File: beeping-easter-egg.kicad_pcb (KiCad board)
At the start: 2 copper layers, 38 x 38 mm, 17 parts, among them Q1 AO3401A, Q2 AO3401A, SW1 YUEN FUNG ST-0-102-A01-T000-LF, U1 TLC555CDR

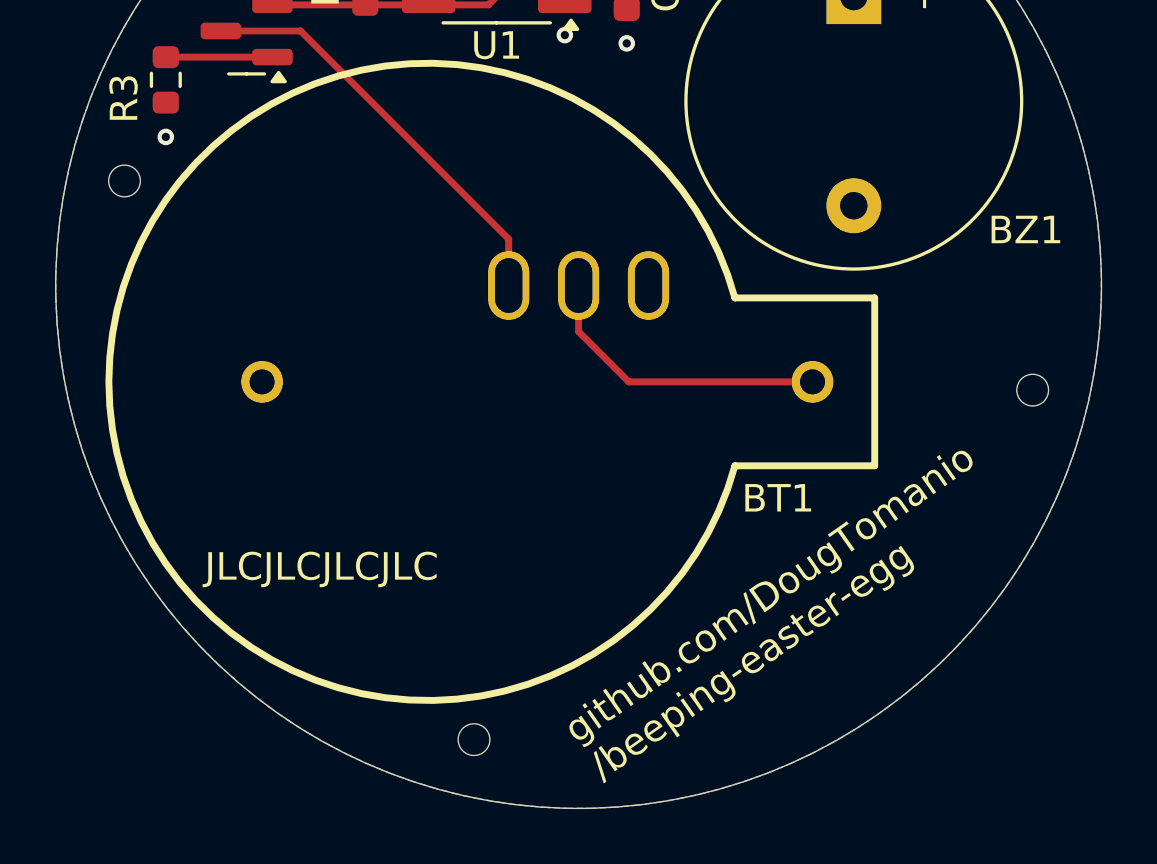
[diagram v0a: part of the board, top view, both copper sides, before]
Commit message: Remove tooling holes. They are added to the panelization frame instead.
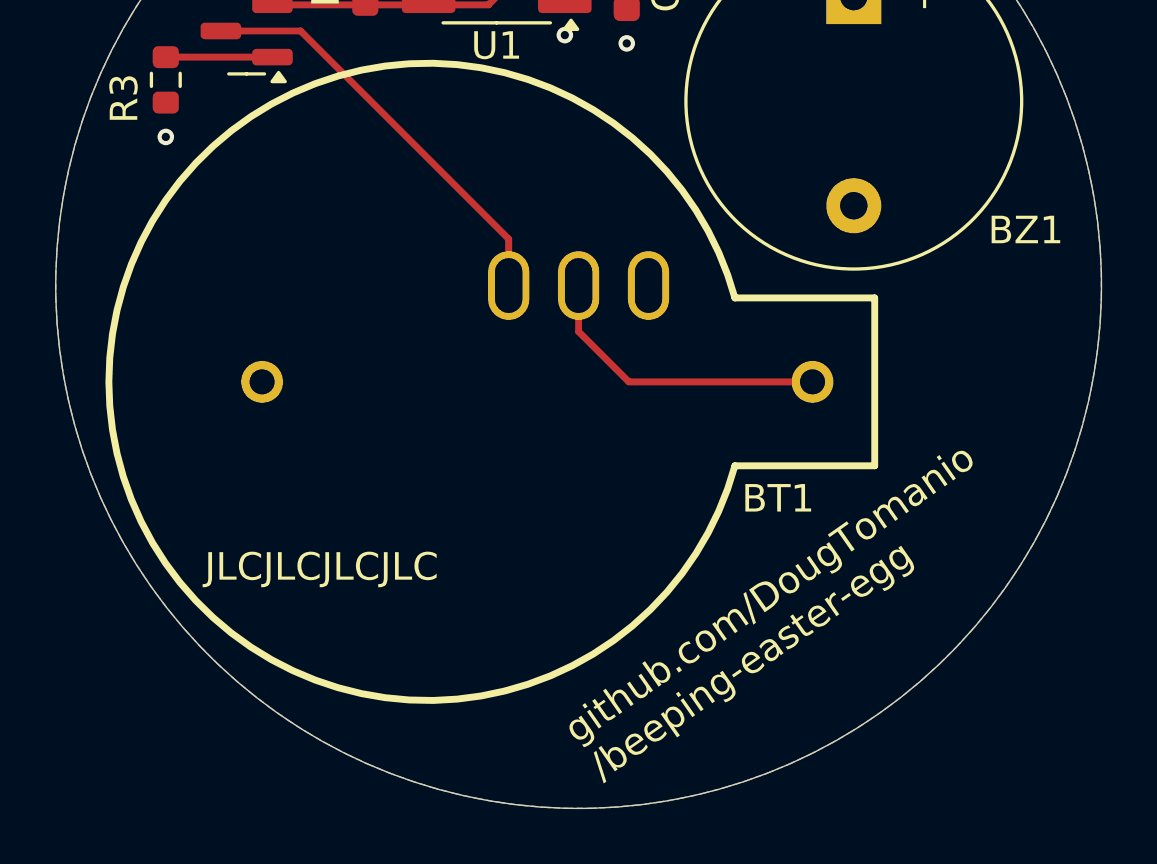
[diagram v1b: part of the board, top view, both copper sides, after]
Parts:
- removed H1, H2, H3: MountingHole, MountingHole:ToolingHole_1.152mm

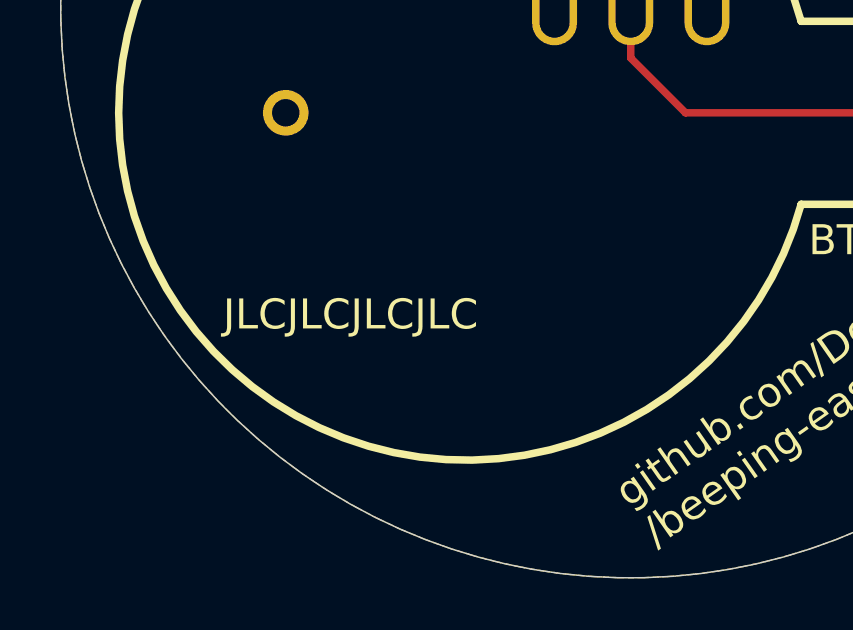
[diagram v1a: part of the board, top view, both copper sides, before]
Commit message: Remove jlc order number placeholder. It is added to the panelization frame instead.
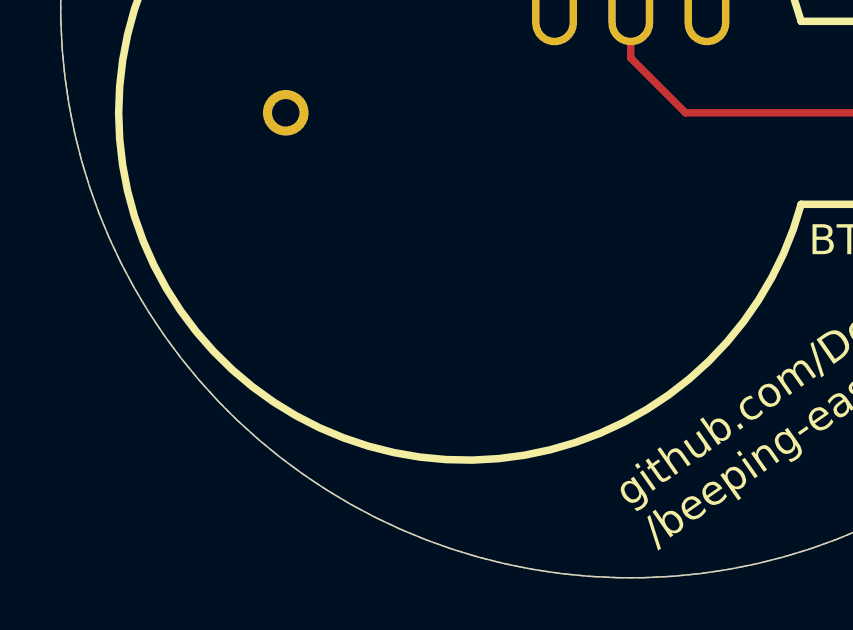
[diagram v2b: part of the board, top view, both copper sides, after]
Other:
- board text removed: "JLCJLCJLCJLC"
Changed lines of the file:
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@@
-		)
-	)
-	(gr_text "JLCJLCJLCJLC"
-		(at 136.41 110.81 0)
-		(layer "F.SilkS")
-		(effects
-			(font
-				(size 1 1)
-				(thickness 0.15)
-			)
-			(justify left bottom)
 		)
 	)

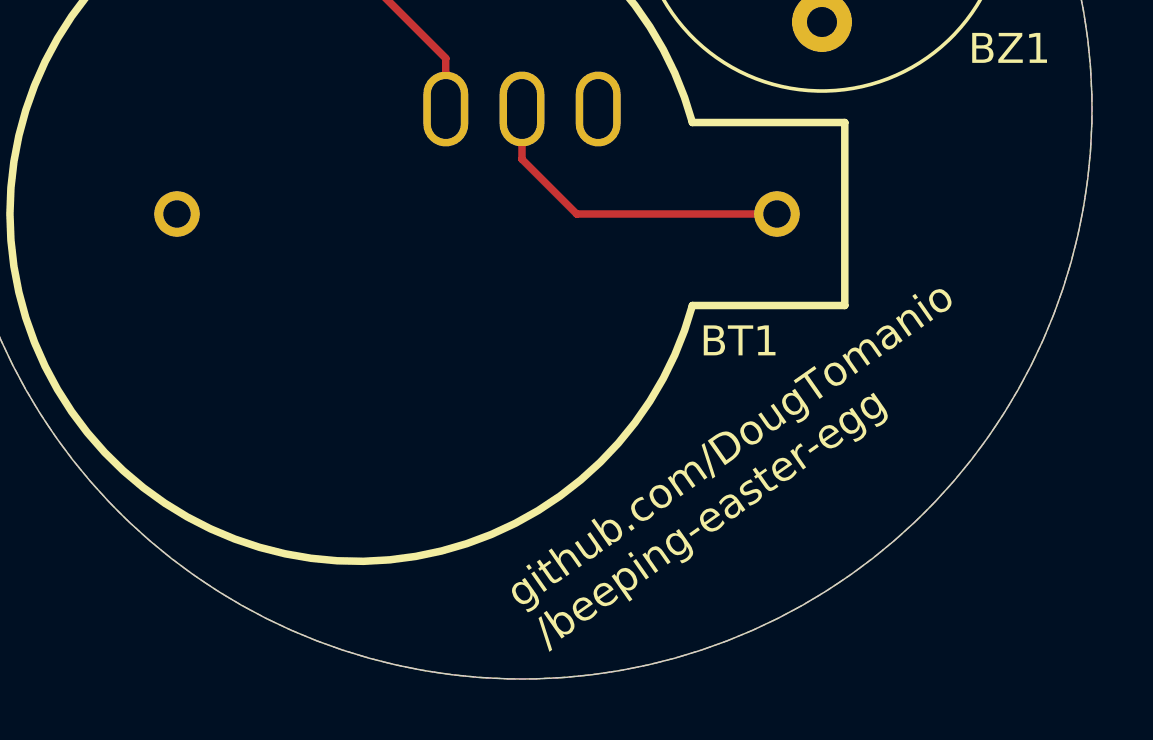
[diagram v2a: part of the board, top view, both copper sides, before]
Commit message: Move label to back copper. Add Rev number.
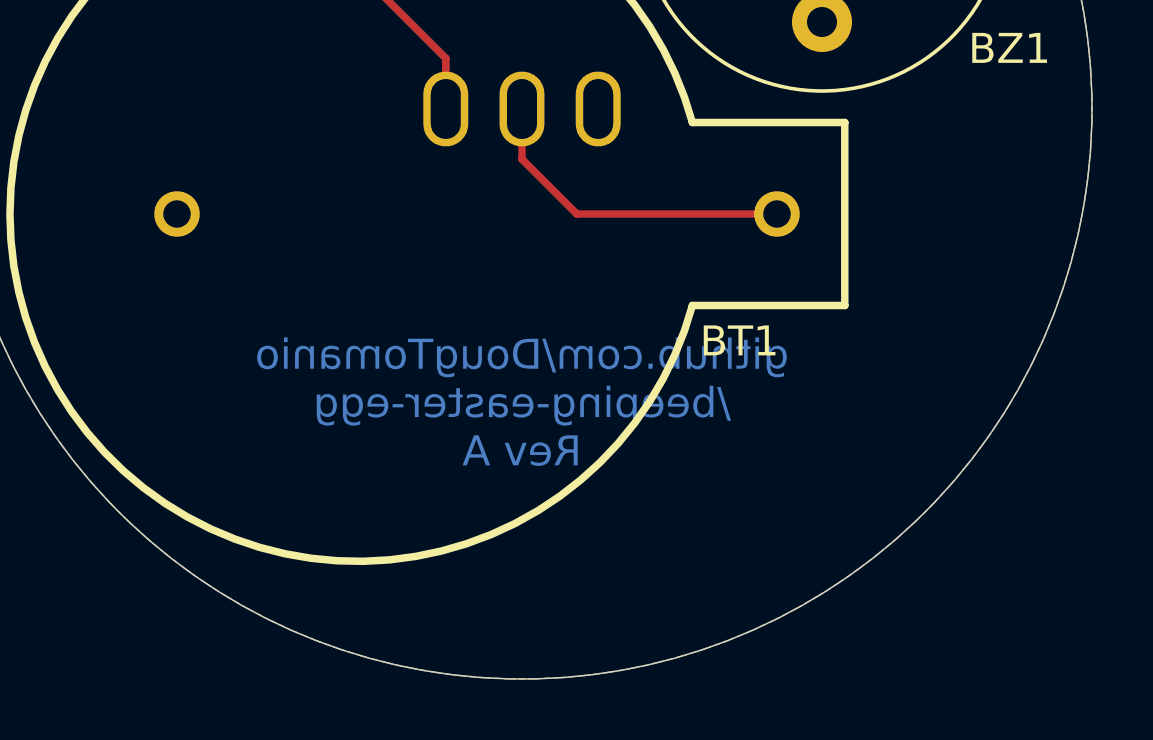
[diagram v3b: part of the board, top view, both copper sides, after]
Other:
- board text added: "github.com/DougTomanio /beeping-easter-egg Rev A"
- board text removed: "github.com/DougTomanio /beeping-easter-egg"
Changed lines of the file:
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@@
 		(layer "Edge.Cuts")
 	)
-	(gr_text "github.com/DougTomanio\n/beeping-easter-egg"
-		(at 150.91 118.09 35)
-		(layer "F.SilkS" knockout)
+	(gr_text "github.com/DougTomanio\n/beeping-easter-egg\nRev A"
+		(at 150 112 0)
+		(layer "B.Cu")
 		(effects
 			(font
@@
 				(thickness 0.15)
 			)
-			(justify left bottom)
+			(justify bottom mirror)
 		)
 	)

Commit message: Set title
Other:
- board text added: "Beeping Easter Egg Rev A"
- board text removed: "github.com/DougTomanio /beeping-easter-egg Rev A"
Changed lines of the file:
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@@
 		(layer "Edge.Cuts")
 	)
-	(gr_text "github.com/DougTomanio\n/beeping-easter-egg\nRev A"
-		(at 150 112 0)
+	(gr_text "Beeping Easter Egg\nRev A"
+		(at 150 111.5 0)
 		(layer "B.Cu")
 		(effects

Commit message: Update component values to reflect corrected timing calculations
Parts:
- R1: value 5.1MΩ -> 10MΩ
- R2: value 10MΩ -> 5.1MΩ
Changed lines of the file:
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@@
 			)
 		)
-		(property "Value" "5.1MΩ"
+		(property "Value" "10MΩ"
 			(at -2.275 -1.25 90)
 			(layer "F.Fab")
@@
 			)
 		)
-		(property "LCSC" "C13320"
+		(property "LCSC" "C7250"
 			(at 0 0 90)
 			(unlocked yes)
@@
 			)
 		)
-		(property "Value" "10MΩ"
+		(property "Value" "5.1MΩ"
 			(at 0 -1.25 90)
 			(layer "F.Fab")
@@
 			)
 		)
-		(property "LCSC" "C7250"
-			(at 0 0 90)
-			(unlocked yes)
+		(property "LCSC" "C13320"
+			(at 0 0 90)
+			(unlocked yes)

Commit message: update rev
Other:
- board text added: "Beeping Easter Egg Rev B"
- board text removed: "Beeping Easter Egg Rev A"
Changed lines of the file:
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@@
 		(layer "Edge.Cuts")
 	)
-	(gr_text "Beeping Easter Egg\nRev A"
+	(gr_text "Beeping Easter Egg\nRev B"
 		(at 150 111.5 0)
 		(layer "B.Cu")

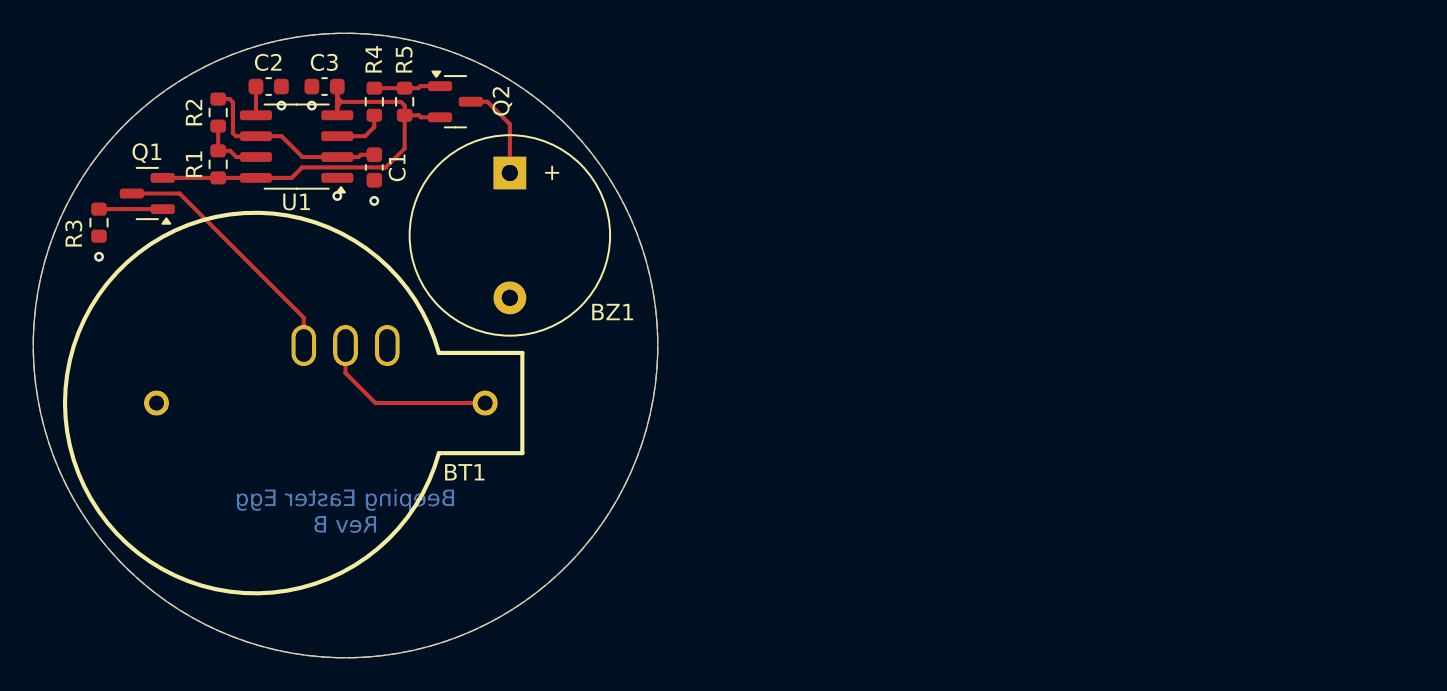
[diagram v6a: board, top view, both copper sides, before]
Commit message: Add cover panel
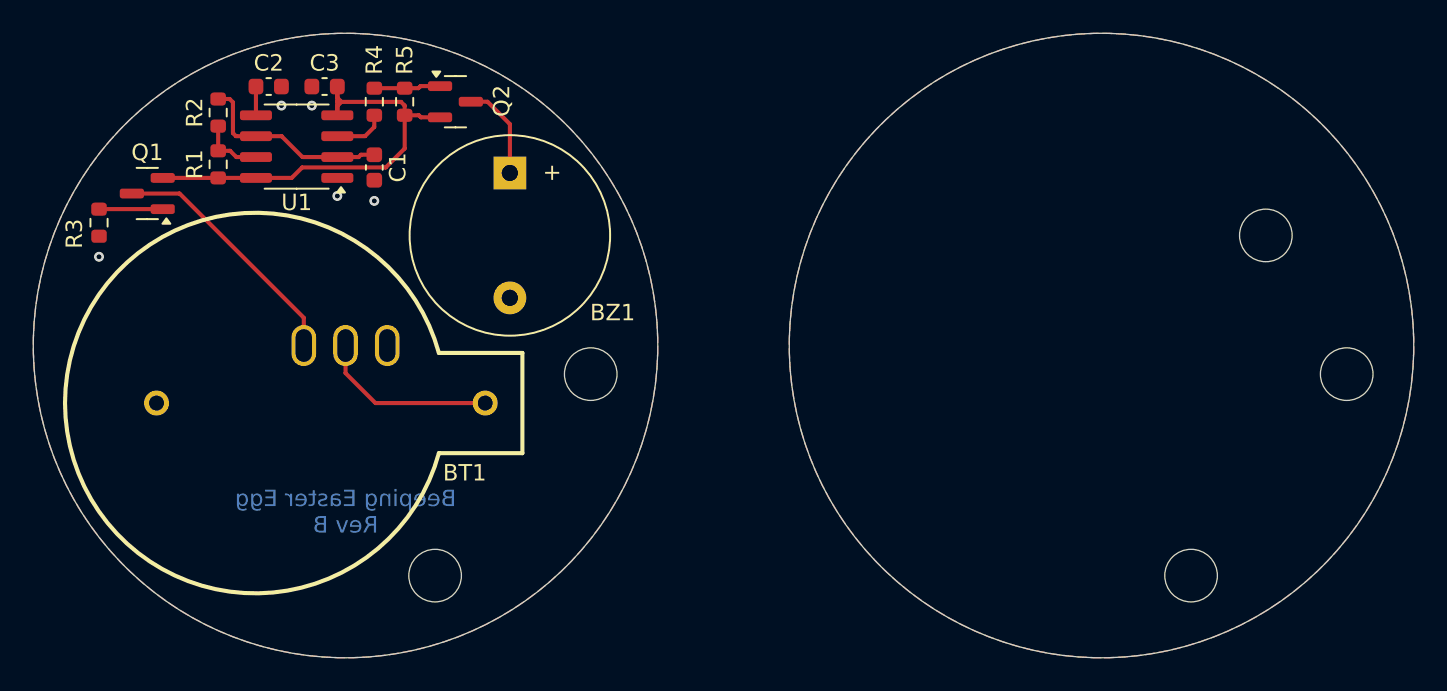
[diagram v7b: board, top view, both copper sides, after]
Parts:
- added REF**: MountingHole_3.2mm_M3, MountingHole:MountingHole_3.2mm_M3, F.Cu at (206.0, 93.3)
- added REF**: MountingHole_3.2mm_M3, MountingHole:MountingHole_3.2mm_M3, F.Cu at (155.4, 114.0)
- added REF**: MountingHole_3.2mm_M3, MountingHole:MountingHole_3.2mm_M3, F.Cu at (201.4, 114.0)
- added REF**: MountingHole_3.2mm_M3, MountingHole:MountingHole_3.2mm_M3, F.Cu at (210.9, 101.7)
- added REF**: MountingHole_3.2mm_M3, MountingHole:MountingHole_3.2mm_M3, F.Cu at (164.9, 101.7)
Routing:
- added copper zone on B.Cu, net (none)
- added copper zone on F.Cu, net (none)
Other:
- board size 38 x 38 mm -> 84 x 38 mm
